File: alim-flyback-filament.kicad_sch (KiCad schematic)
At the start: 0 parts

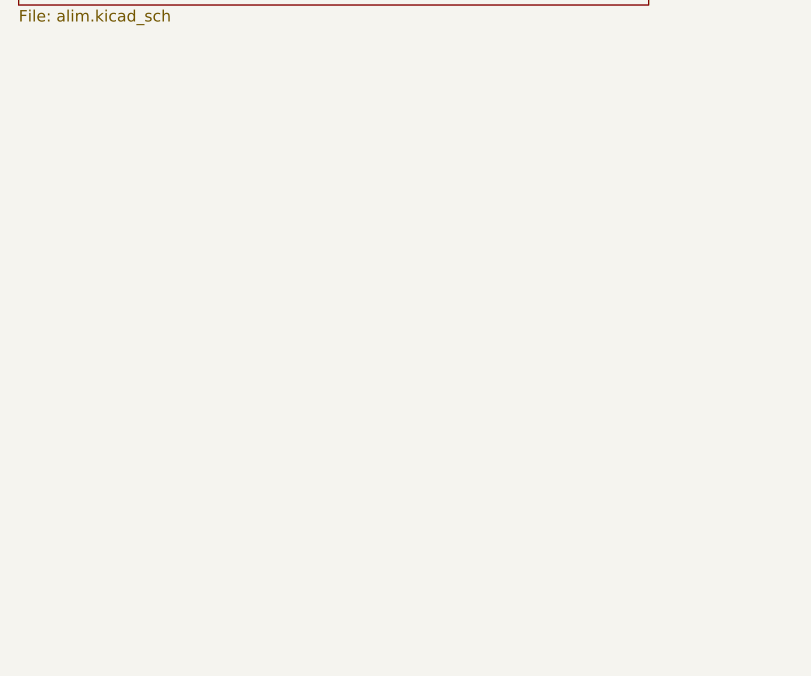
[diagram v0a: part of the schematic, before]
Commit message: Isolation C2000 réelle (GND_CTRL/3V3_CTRL) + feuille Polarisation (HV_BIAS actif 0-90V)
- U3/U4/U5/U7/U8/U9 migrés côté contrôle vers GND_CTRL/3V3_CTRL (isolation
  du C2000 réellement effective, plus seulement nominale)
- Connecteurs CpuOut/CpuIn agrandis 2x04→2x08 (16 broches), marge pour
  futurs signaux et compatibilité avec d'autres cartes
- Nouvelle feuille polarisation.kicad_sch : pilotage actif de HV_BIAS
  (point de polarisation du secondaire flottant) depuis une alimentation
  400V externe — source de courant 300µA (BSS127I+MMBT2222), MOSFET
  variable BSS127I piloté par PWM isolé (ISO7710), protection TVS +
  pull-up grille, retour mesure isolé (AMC0311R)
- Nouveaux symboles custom BSS127I/MMBT2222, empreinte SOIC_DWV partagée
  par les amplis isolés de la famille AMC03x1R/AMC03x2R

Co-Authored-By: Claude Sonnet 5 <noreply@anthropic.com>
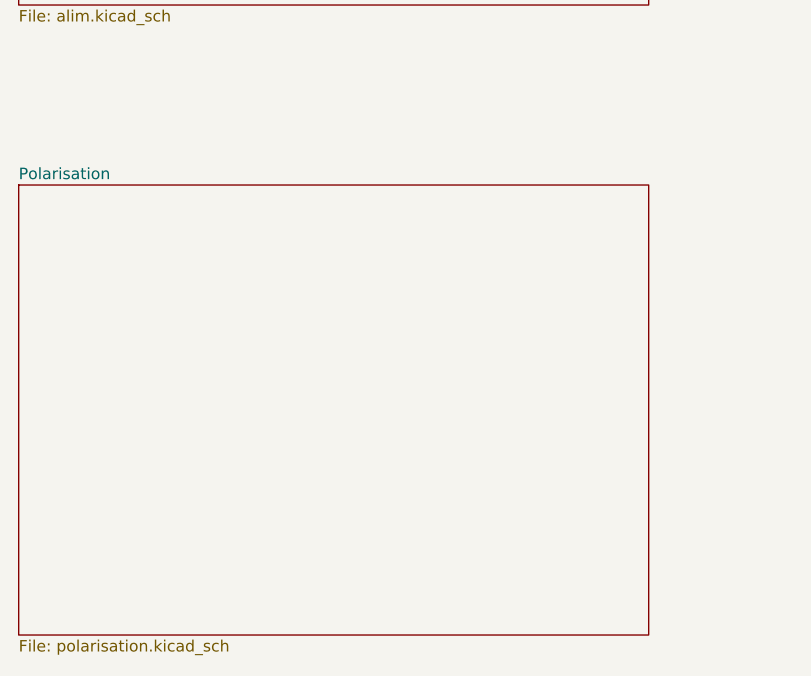
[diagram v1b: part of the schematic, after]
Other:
- added sheet Polarisation (polarisation.kicad_sch)
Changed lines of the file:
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@@
+		)
+	)
+	(sheet
+		(at 20 90)
+		(size 70 50)
+		(exclude_from_sim no)
+		(in_bom yes)
+		(on_board yes)
+		(dnp no)
+		(fields_autoplaced yes)
+		(stroke
+			(width 0.1524)
+			(type solid)
+		)
+		(fill
+			(color 0 0 0 0)
+		)
+		(property "Sheetname" "Polarisation"
+			(at 20 89.5 0)
+			(show_name no)
+			(do_not_autoplace no)
+			(effects
+				(font
+					(size 1.27 1.27)
+				)
+				(justify left bottom)
+			)
+		)
+		(property "Sheetfile" "polarisation.kicad_sch"
+			(at 20 140.5 0)
+			(show_name no)
+			(do_not_autoplace no)
+			(effects
+				(font
+					(size 1.27 1.27)
+				)
+				(justify left top)
+			)
+		)
+		(instances
+			(project "alim-flyback-filament"
+				(path "/c8449ac7-87b3-4a93-889f-06dd686c5aff"
+					(page "5")
+				)
+			)
 		)
 	)
